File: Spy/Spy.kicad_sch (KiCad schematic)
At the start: 8 parts, among them J1 Screw_Terminal_01x02, J2 Screw_Terminal_01x02, U1 ESP32-DevKitC, U2 GP2Y0A21YK0F, U3 GP2Y0A21YK0F, U4 SEN-12787, U5 L298N, U6 QTR-8A

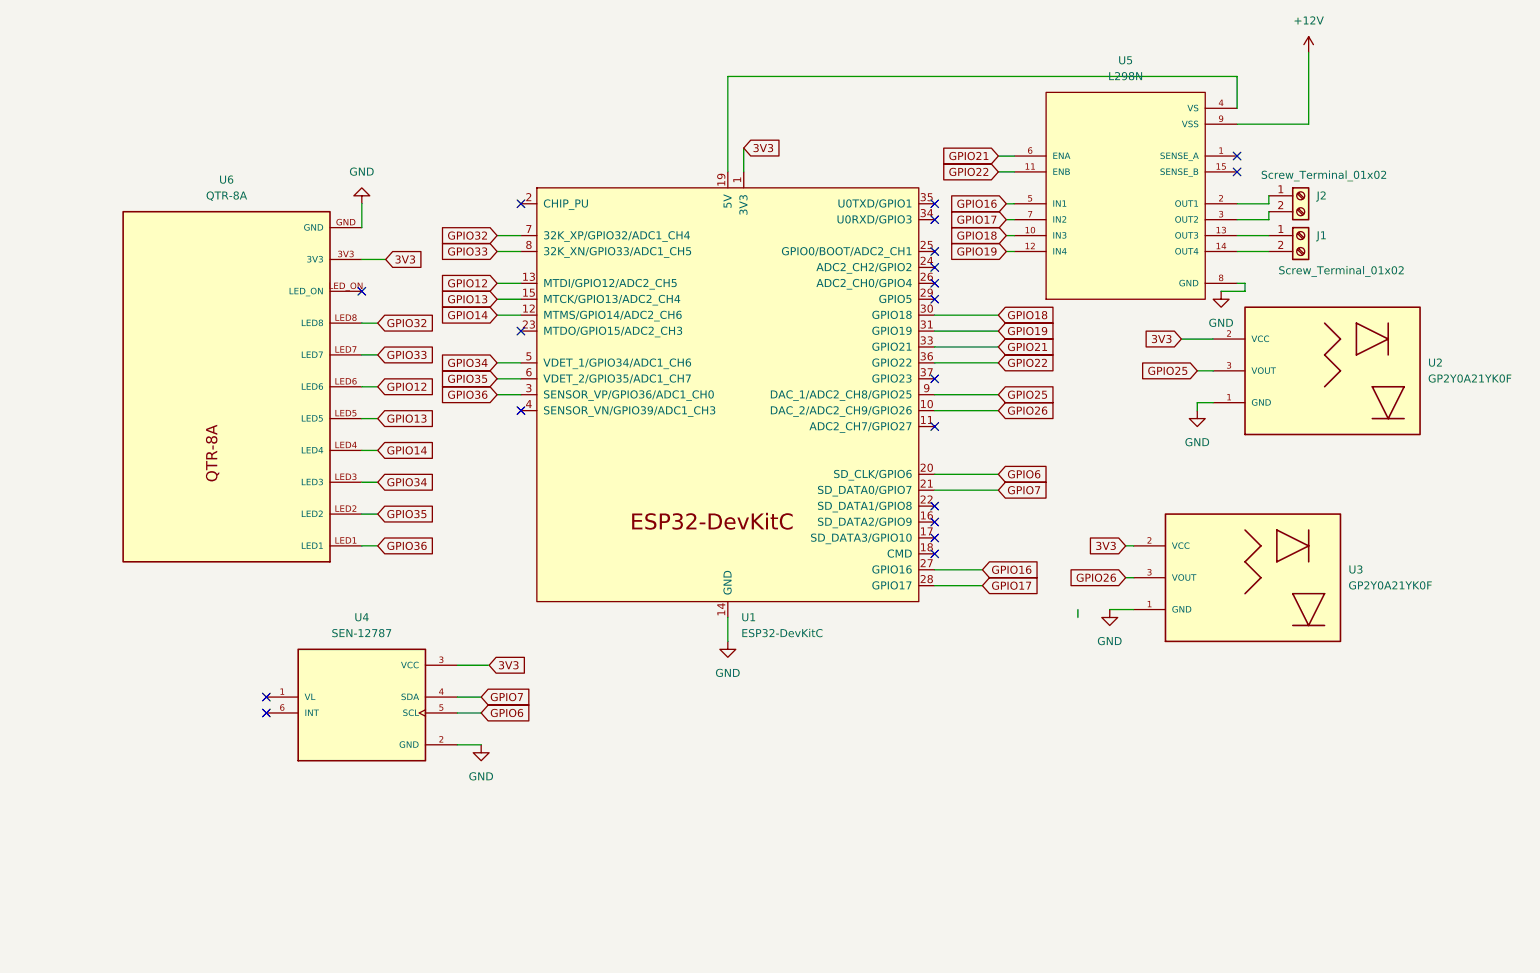
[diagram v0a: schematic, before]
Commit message: DRV8871 driver and pin rewiring
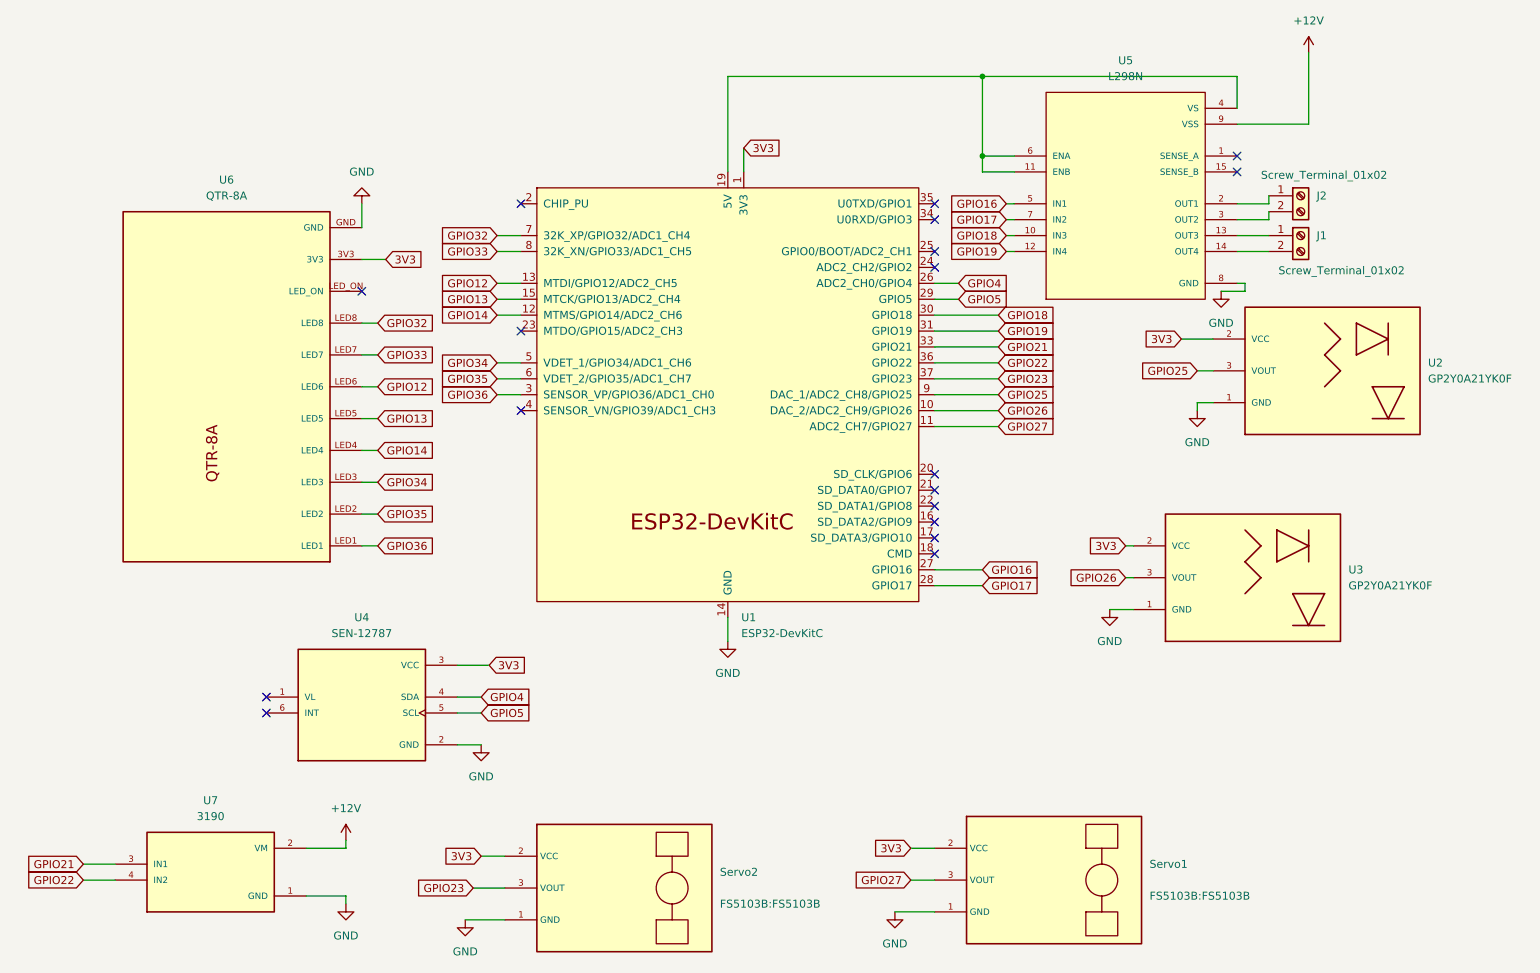
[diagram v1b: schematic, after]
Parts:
- added Servo1, Servo2: ~, FS5103B:FS5103B, symbol FS5103B:FS5103B
- added U7: 3190, 3190:MODULE_3190, symbol 3190:3190
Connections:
- net +12V: now also U7.2 (VM)
- net 3V3: now also Servo1.2 (VCC), Servo2.2 (VCC)
- net GND: now also Servo1.1 (GND), Servo2.1 (GND), U7.1 (GND)
- net GPIO21: now also U7.3 (IN1); no longer U5.6 (ENA)
- net GPIO22: now also U7.4 (IN2); no longer U5.11 (ENB)
- net GPIO27: now reaches U1.11 (ADC2_CH7/GPIO27)
- net GPIO27: now also Servo1.3 (VOUT)
- net at U1.19 (5V), U5.4 (VS): now also U5.11 (ENB), U5.6 (ENA)
- net GPIO4: now reaches U1.26 (ADC2_CH0/GPIO4)
- net GPIO4: now also U4.4 (SDA)
- net GPIO5: now reaches U1.29 (GPIO5)
- net GPIO5: now also U4.5 (SCL)
- net GPIO23: now reaches U1.37 (GPIO23)
- net GPIO23: now also Servo2.3 (VOUT)
- net GPIO6: no longer names the net of U1.20 (SD_CLK/GPIO6)
- net GPIO6: no longer U4.5 (SCL)
- net GPIO7: no longer names the net of U1.21 (SD_DATA0/GPIO7)
- net GPIO7: no longer U4.4 (SDA)
- no-connect marks 20 -> 18

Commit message: rewired some stuff
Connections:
- net GPIO21: now also U4.4 (SDA); no longer U7.3 (IN1)
- net GPIO22: now also U4.5 (SCL); no longer U7.4 (IN2)
- net GPIO4: now also U7.3 (IN1); no longer U4.4 (SDA)
- net GPIO5: now also U7.4 (IN2); no longer U4.5 (SCL)

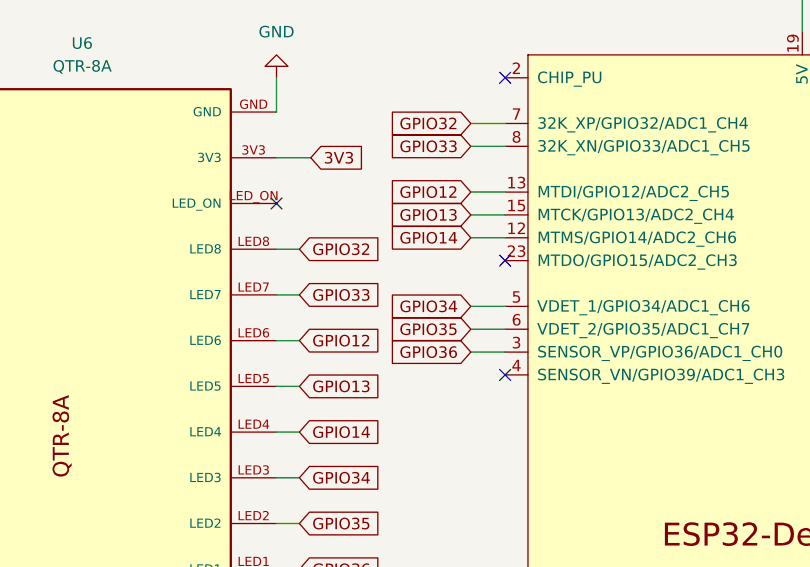
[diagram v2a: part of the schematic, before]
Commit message: Reverted and fixed version of code. Some minor PCB updates
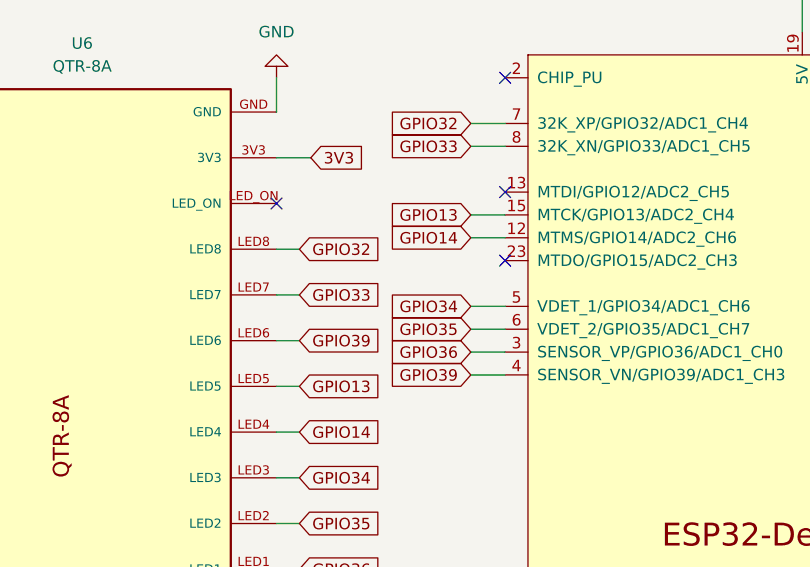
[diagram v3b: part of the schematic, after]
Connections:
- net GPIO39: now reaches U1.4 (SENSOR_VN/GPIO39/ADC1_CH3)
- net GPIO39: now also U6.LED6
- net GPIO12: no longer names the net of U1.13 (MTDI/GPIO12/ADC2_CH5)
- net GPIO12: no longer U6.LED6
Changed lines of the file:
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@@
-	)
-	(no_connect
-		(at 119.38 76.2)
 	)
 	(no_connect
@@
 	)
 	(no_connect
+		(at 119.38 55.88)
+	)
+	(no_connect
 		(at 233.68 38.1)
 	)
@@
 	(wire
 		(pts
-			(xy 115.57 55.88) (xy 119.38 55.88)
-		)
-		(stroke
-			(width 0)
-			(type default)
-		)
-	)
-	(wire
-		(pts
 			(xy 193.04 22.86) (xy 193.04 35.56)
 		)
@@
 	(wire
 		(pts
+			(xy 115.57 76.2) (xy 119.38 76.2)
+		)
+		(stroke
+			(width 0)
+			(type default)
+		)
+	)
+	(wire
+		(pts
 			(xy 233.68 43.18) (xy 238.76 43.18)
 		)
@@
 		)
 	)
-	(global_label "GPIO12"
+	(global_label "GPIO39"
 		(shape input)
 		(at 96.52 72.39 0)
@@
 		)
 	)
-	(global_label "GPIO12"
-		(shape input)
-		(at 115.57 55.88 180)
+	(global_label "GPIO39"
+		(shape input)
+		(at 115.57 76.2 180)
 		(fields_autoplaced yes)
 		(effects
@@
 		)
 		(property "Intersheetrefs" "${INTERSHEET_REFS}"
-			(at 105.6905 55.88 0)
-			(effects
-				(font
+			(at 105.6905 76.2 0)
+			(effects
+				(font
